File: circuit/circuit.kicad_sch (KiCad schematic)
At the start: 23 parts

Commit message: .
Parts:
- removed BT?: CR2302, symbol Device:Battery_Cell
- removed C?: 0.1uF, symbol Device:C
- removed U?: DS1302+, Package_DIP:DIP-8_W7.62mm, symbol Timer_RTC:DS1302+
- removed Y?: 32.768 kHz, symbol Device:Crystal_Small
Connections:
- net RT_CE: no longer names the net of J?.8 (Pin_8)
- net RT_IO: no longer names the net of J?.7 (Pin_7)
- net RT_SCLK: no longer names the net of J?.9 (Pin_9)
- no-connect marks 15 -> 18
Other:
- note removed: "Real time clock"
- moved on the sheet: DS?, J?, R?, RV?, SW?

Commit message: .
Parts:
- added D?: LED, symbol Device:LED
- added Q?: 2N3906, Package_TO_SOT_THT:TO-92_Inline, symbol Transistor_BJT:2N3906
- added R?: 1K, symbol Device:R
- added R?: 4K7, symbol Device:R
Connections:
- net +5V: now also Q?.1 (E)
- net GND: now also D?.1 (K)
- net SD_CS: now also R?.1
- new net: D?.2 (A), R?.2
- new net: Q?.3 (C), R?.1
- new net: Q?.2 (B), R?.2
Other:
- moved on the sheet: J?

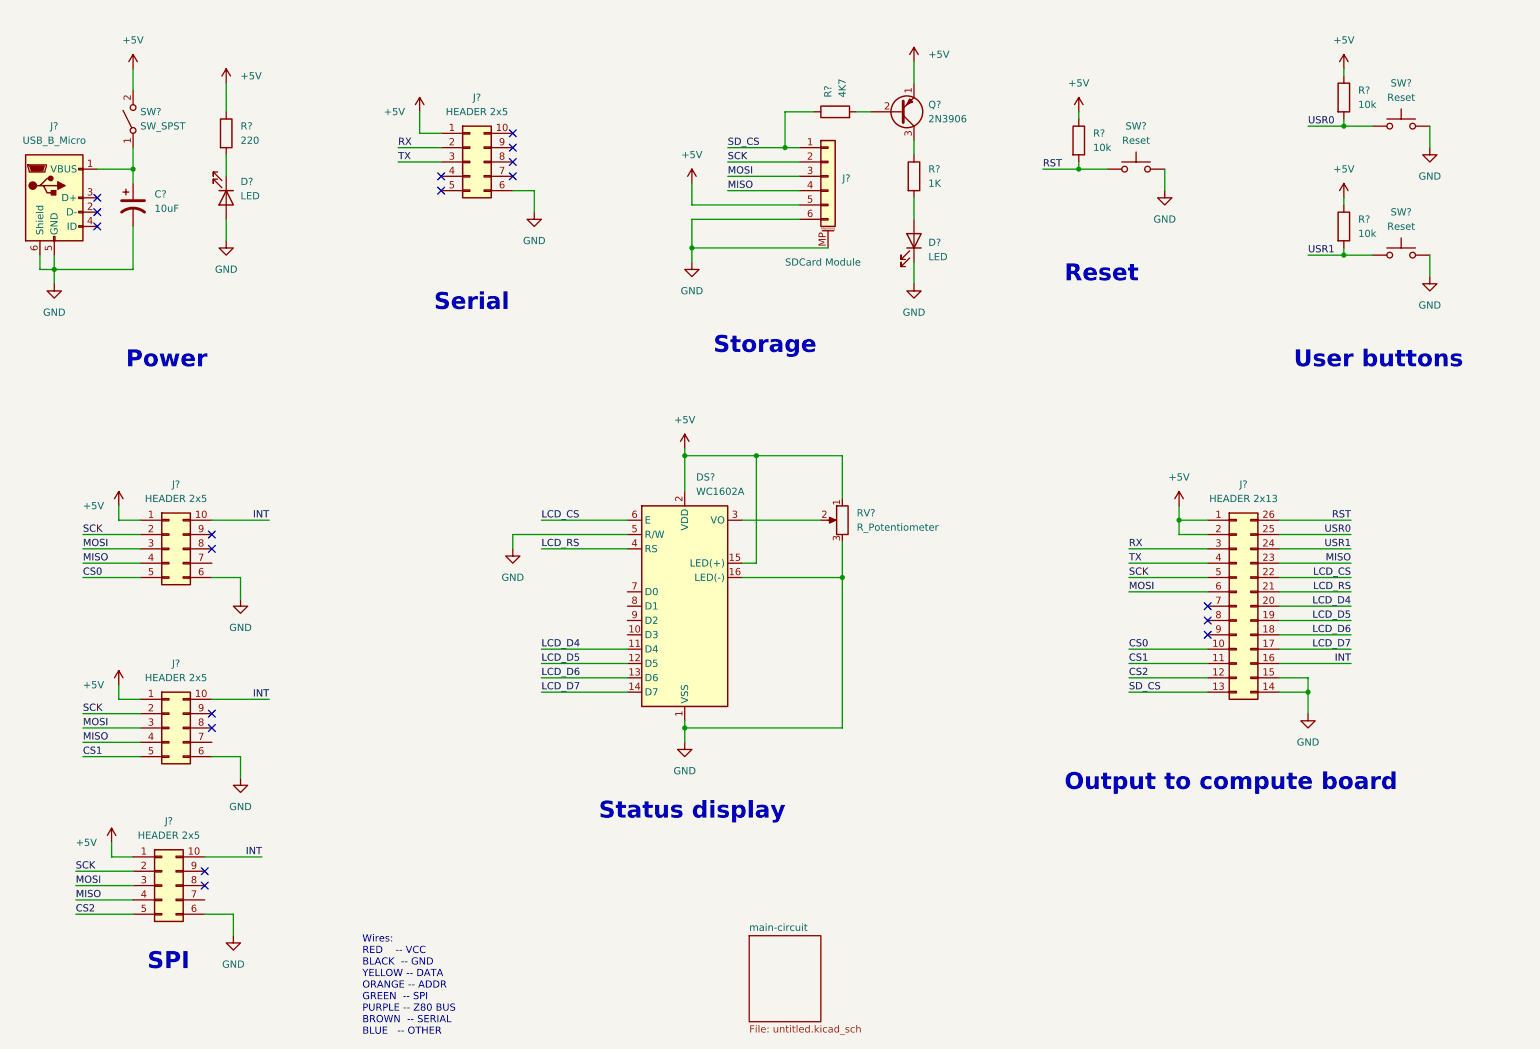
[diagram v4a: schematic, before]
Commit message: Schematic changes
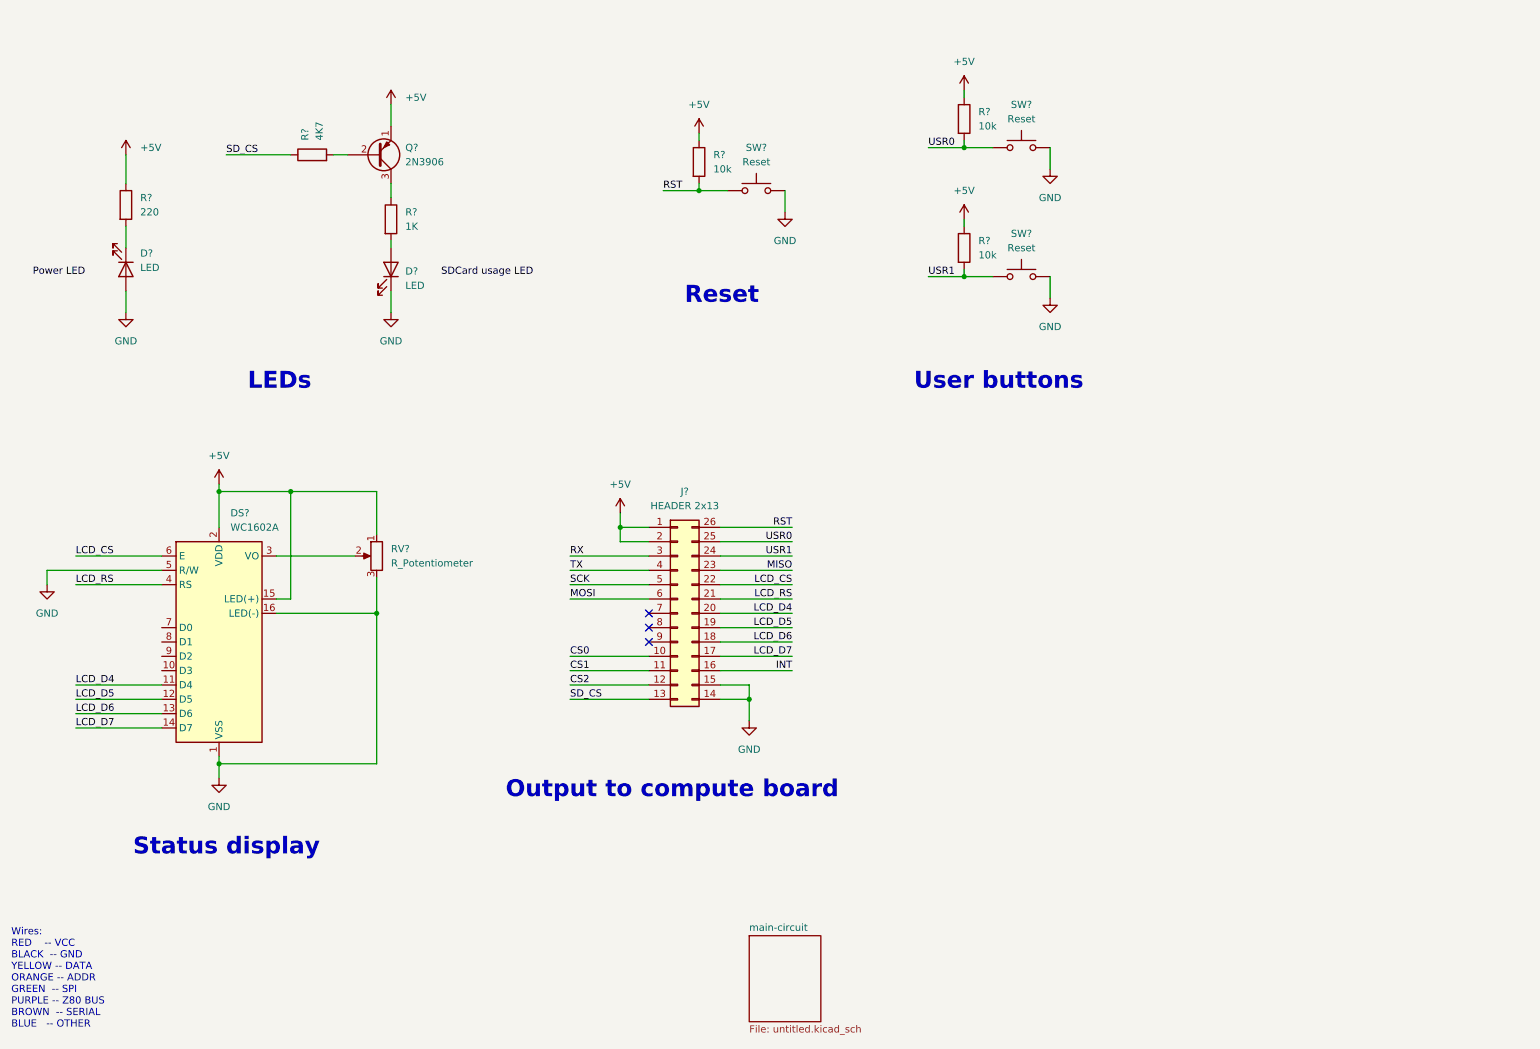
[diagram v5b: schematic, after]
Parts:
- removed C?: 10uF, symbol Device:C_Polarized_US
- removed J?: SDCard Module, symbol Connector_Generic_MountingPin:Conn_01x06_MountingPin
- removed J? (x4): HEADER 2x5, symbol Connector_Generic:Conn_02x05_Counter_Clockwise
- removed J?: USB_B_Micro, symbol Connector:USB_B_Micro
- removed SW?: SW_SPST, symbol Switch:SW_SPST
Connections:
- no-connect marks 18 -> 3
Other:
- note added: "LEDs"
- note removed: "Power"
- note removed: "SPI"
- note removed: "Serial"
- note removed: "Storage"
- moved on the sheet: D?, DS?, J?, Q?, R?, RV?, SW?

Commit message: WIP
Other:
- note added: "Main board ->"
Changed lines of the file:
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@@
     (effects (font (size 3 3) (thickness 0.6) bold) (justify left bottom))
+  )
+  (text "Main board ->" (at 111.76 186.69 0)
+    (effects (font (size 3 3)) (justify left bottom))
   )
   (text "Wires:\nRED    -- VCC\nBLACK  -- GND\nYELLOW -- DATA\nORANGE -- ADDR\nGREEN  -- SPI\nPURPLE -- Z80 BUS\nBROWN  -- SERIAL\nBLUE   -- OTHER"
@@
       (reference "#PWR?") (unit 1) (value "+5V") (footprint "")
     )
+    (path "/e9d70090-90fc-4e9b-9b66-2c4a5e914581/8667c096-1105-4282-abf5-b5f5fd5d95a1"
+      (reference "#PWR?") (unit 1) (value "+3V3") (footprint "")
+    )
     (path "/e9d70090-90fc-4e9b-9b66-2c4a5e914581/883247fb-bfb5-42ae-8659-a110c018d3aa"
       (reference "#PWR?") (unit 1) (value "+5V") (footprint "")
@@
       (reference "#PWR?") (unit 1) (value "+5V") (footprint "")
     )
+    (path "/e9d70090-90fc-4e9b-9b66-2c4a5e914581/ea43ba8b-e61d-4888-aa80-16b0815f20c3"
+      (reference "#PWR?") (unit 1) (value "+5V") (footprint "")
+    )
     (path "/e9d70090-90fc-4e9b-9b66-2c4a5e914581/eac37082-9088-47ba-ac7c-ed45350bdf21"
       (reference "#PWR?") (unit 1) (value "+5V") (footprint "")
@@
       (reference "U?") (unit 1) (value "ATmega2560-16A") (footprint "Package_QFP:TQFP-100_14x14mm_P0.5mm")
     )
+    (path "/e9d70090-90fc-4e9b-9b66-2c4a5e914581/e6bc2f02-5b3d-4456-a918-ddd7fc18f8e5"
+      (reference "U?") (unit 1) (value "Level shifter") (footprint "Package_SO:TSSOP-14_4.4x5mm_P0.65mm")
+    )
     (path "/e9d70090-90fc-4e9b-9b66-2c4a5e914581/b78b446a-b4b4-477c-99a7-ae017f47fd2e"
